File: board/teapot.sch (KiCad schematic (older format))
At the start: 31 parts

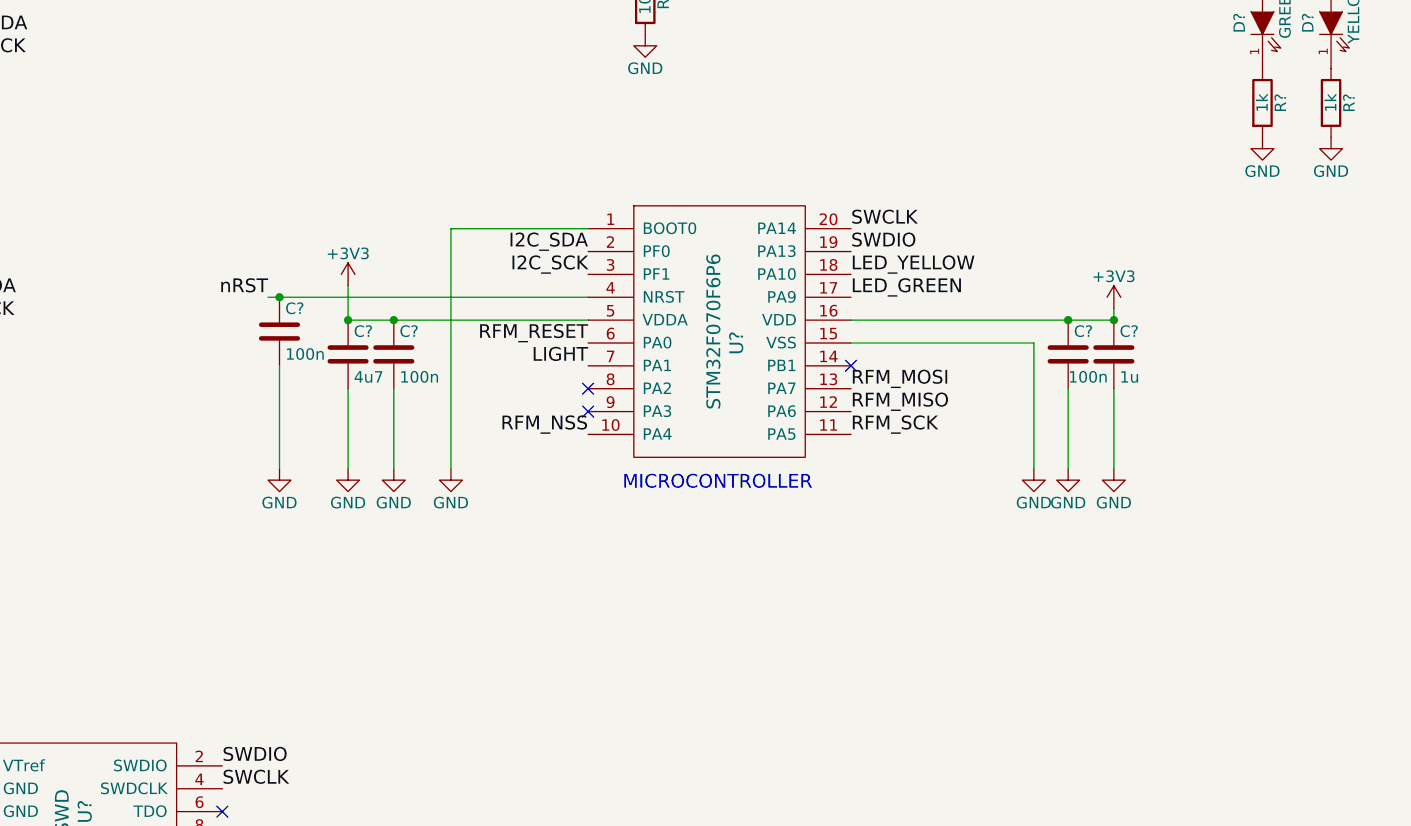
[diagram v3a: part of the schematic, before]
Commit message: Changed stm32f070 to stm32l052k8u6
Also did mcu decouplers properly
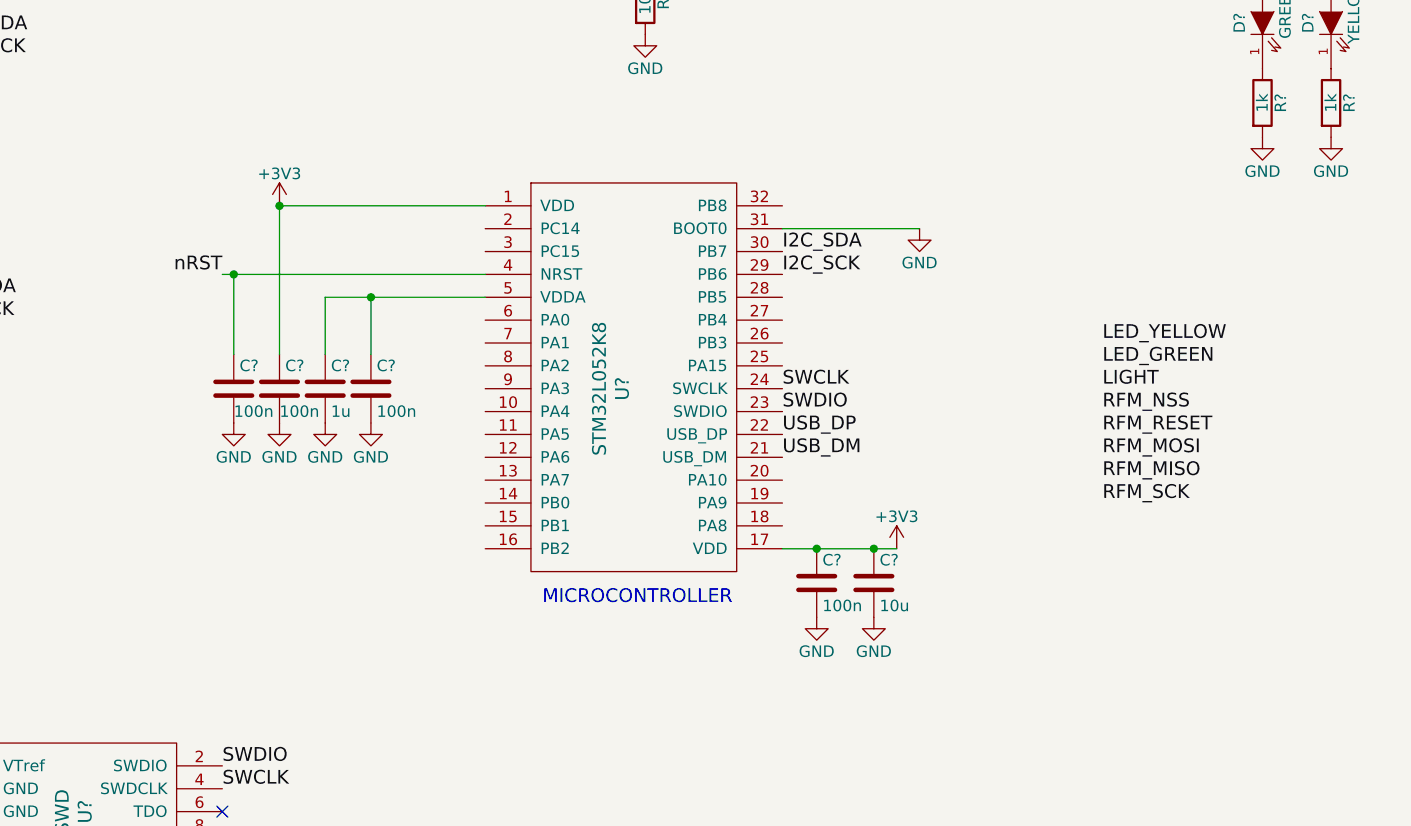
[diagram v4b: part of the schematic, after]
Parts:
- removed C? (x3): 100n, symbol C
- removed C?: 1u, symbol C
- removed C?: 4u7, symbol C
- removed U?: STM32F070F6P6, symbol STM32F070F6P6
- added C? (x4): 100n, symbol C
- added C?: 10u, symbol C
- added C?: 1u, symbol C
- added U?: STM32L052K8, symbol STM32L052K8
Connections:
- net +3V3: now also C?.1, C?.1, C?.1, U?.1 (VDD), U?.17 (VDD)
- net GND: now also C?.2, C?.2, C?.2, C?.2, C?.2, C?.2, U?.31 (BOOT0)
- net I2C_SCK: now also U?.29 (PB6)
- net I2C_SDA: now also U?.30 (PB7)
- net SWCLK: now also U?.24 (SWCLK)
- net SWDIO: now also U?.23 (SWDIO)
- net nRST: now also C?.1, U?.4 (NRST)
- new net: C?.1, C?.1, U?.5 (VDDA)
- new net USB_DM: U?.21 (USB_DM)
- new net USB_DP: U?.22 (USB_DP)
- no-connect marks 11 -> 8

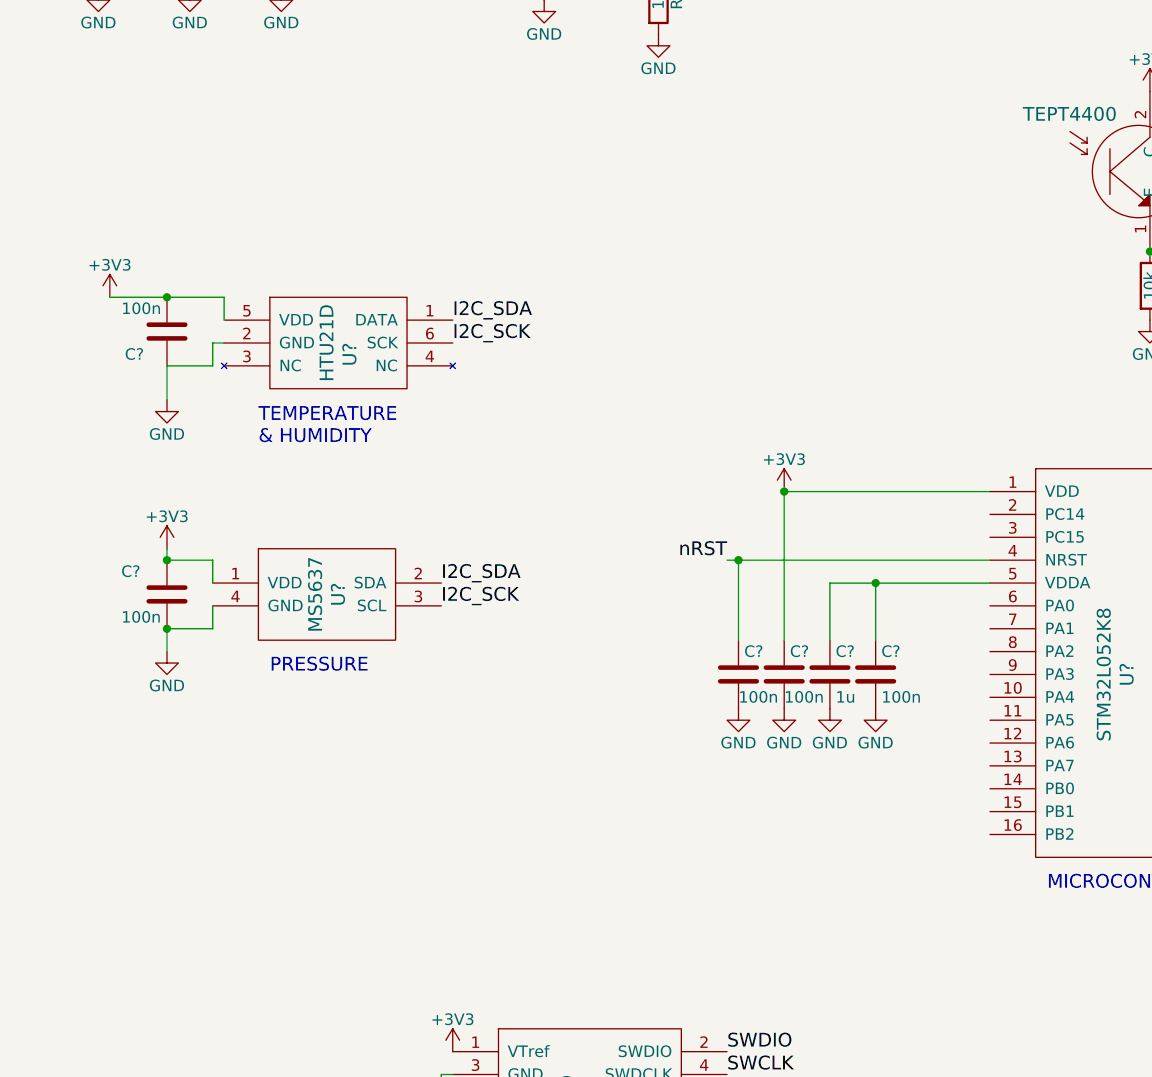
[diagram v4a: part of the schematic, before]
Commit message: Added watch crystal
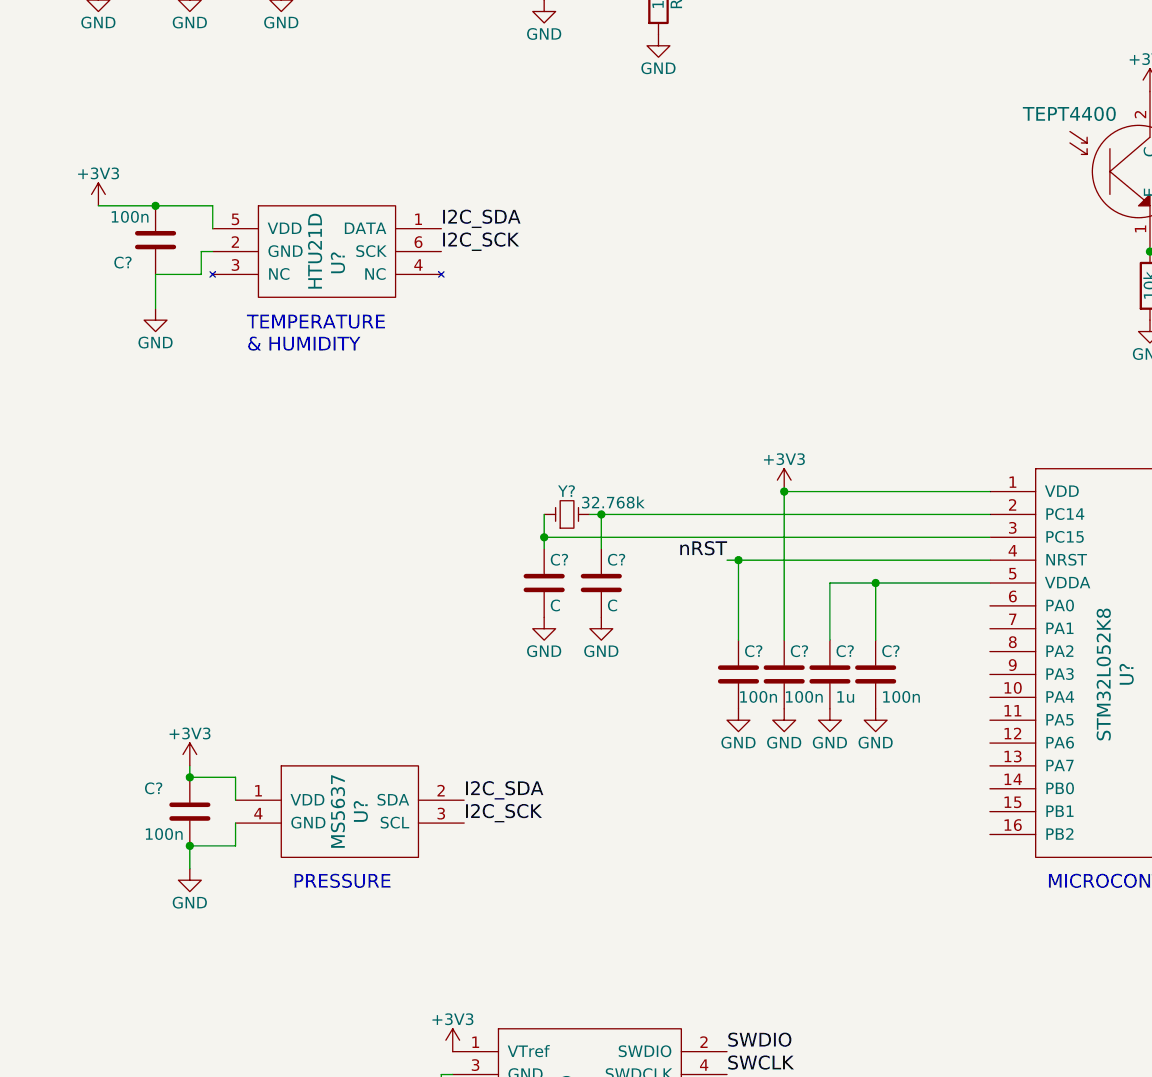
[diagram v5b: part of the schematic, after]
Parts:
- added C? (x2): C, symbol C
- added Y?: 32.768k, symbol Crystal_Small
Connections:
- net GND: now also C?.2, C?.2
- net at U?.2 (PC14): now also C?.1, Y?.2
- net at U?.3 (PC15): now also C?.1, Y?.1
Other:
- moved on the sheet: C?, U?
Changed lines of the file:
@@
 L C C?
 U 1 1 56707B80
-P 1300 3250
-F 0 "C?" H 1400 3350 50  0000 L CNN
-F 1 "100n" H 1325 3150 50  0000 L CNN
-F 2 "" H 1338 3100 50  0000 C CNN
-F 3 "" H 1300 3250 50  0000 C CNN
-	1    1300 3250
+P 1250 2850
+F 0 "C?" H 1350 2950 50  0000 L CNN
+F 1 "100n" H 1275 2750 50  0000 L CNN
+F 2 "" H 1288 2700 50  0000 C CNN
+F 3 "" H 1250 2850 50  0000 C CNN
+	1    1250 2850
 	-1   0    0    1
 $EndComp
@@
 L HTU21D U?
 U 1 1 5670851D
-P 2050 3300
-F 0 "U?" V 2100 3250 60  0000 C CNN
-F 1 "HTU21D" V 2000 3300 60  0000 C CNN
-F 2 "" H 2100 3350 60  0000 C CNN
-F 3 "" H 2100 3350 60  0000 C CNN
-F 4 "2393536" H 2050 3300 60  0001 C CNN "Farnell"
-	1    2050 3300
+P 2000 2900
+F 0 "U?" V 2050 2850 60  0000 C CNN
+F 1 "HTU21D" V 1950 2900 60  0000 C CNN
+F 2 "" H 2050 2950 60  0000 C CNN
+F 3 "" H 2050 2950 60  0000 C CNN
+F 4 "2393536" H 2000 2900 60  0001 C CNN "Farnell"
+	1    2000 2900
 	1    0    0    -1
 $EndComp
@@
 L +3V3 #PWR?
 U 1 1 56708637
-P 1050 3100
-F 0 "#PWR?" H 1050 2950 50  0001 C CNN
-F 1 "+3V3" H 1050 3240 50  0000 C CNN
-F 2 "" H 1050 3100 50  0000 C CNN
-F 3 "" H 1050 3100 50  0000 C CNN
-	1    1050 3100
+P 1000 2700
+F 0 "#PWR?" H 1000 2550 50  0001 C CNN
+F 1 "+3V3" H 1000 2840 50  0000 C CNN
+F 2 "" H 1000 2700 50  0000 C CNN
+F 3 "" H 1000 2700 50  0000 C CNN
+	1    1000 2700
 	1    0    0    -1
 $EndComp
@@
 L GND #PWR?
 U 1 1 5670867A
-P 1300 3550
-F 0 "#PWR?" H 1300 3300 50  0001 C CNN
-F 1 "GND" H 1300 3400 50  0000 C CNN
-F 2 "" H 1300 3550 50  0000 C CNN
-F 3 "" H 1300 3550 50  0000 C CNN
-	1    1300 3550
+P 1250 3150
+F 0 "#PWR?" H 1250 2900 50  0001 C CNN
+F 1 "GND" H 1250 3000 50  0000 C CNN
+F 2 "" H 1250 3150 50  0000 C CNN
+F 3 "" H 1250 3150 50  0000 C CNN
+	1    1250 3150
 	1    0    0    -1
 $EndComp
@@
 L MS5637 U?
 U 1 1 56708DE8
-P 2000 4400
-F 0 "U?" V 2050 4400 60  0000 C CNN
-F 1 "MS5637" V 1950 4400 60  0000 C CNN
-F 2 "" H 1900 4550 60  0000 C CNN
-F 3 "" H 1900 4550 60  0000 C CNN
-	1    2000 4400
+P 2100 5350
+F 0 "U?" V 2150 5350 60  0000 C CNN
+F 1 "MS5637" V 2050 5350 60  0000 C CNN
+F 2 "" H 2000 5500 60  0000 C CNN
+F 3 "" H 2000 5500 60  0000 C CNN
+	1    2100 5350
 	1    0    0    -1
 $EndComp
@@
 L C C?
 U 1 1 56708EC5
-P 1300 4400
-F 0 "C?" H 1100 4500 50  0000 L CNN
-F 1 "100n" H 1100 4300 50  0000 L CNN
-F 2 "" H 1338 4250 50  0000 C CNN
-F 3 "" H 1300 4400 50  0000 C CNN
-	1    1300 4400
+P 1400 5350
+F 0 "C?" H 1200 5450 50  0000 L CNN
+F 1 "100n" H 1200 5250 50  0000 L CNN
+F 2 "" H 1438 5200 50  0000 C CNN
+F 3 "" H 1400 5350 50  0000 C CNN
+	1    1400 5350
 	1    0    0    -1
 $EndComp
@@
 L +3V3 #PWR?
 U 1 1 56708F0F
-P 1300 4200
-F 0 "#PWR?" H 1300 4050 50  0001 C CNN
-F 1 "+3V3" H 1300 4340 50  0000 C CNN
-F 2 "" H 1300 4200 50  0000 C CNN
-F 3 "" H 1300 4200 50  0000 C CNN
-	1    1300 4200
+P 1400 5150
+F 0 "#PWR?" H 1400 5000 50  0001 C CNN
+F 1 "+3V3" H 1400 5290 50  0000 C CNN
+F 2 "" H 1400 5150 50  0000 C CNN
+F 3 "" H 1400 5150 50  0000 C CNN
+	1    1400 5150
 	1    0    0    -1
 $EndComp
@@
 L GND #PWR?
 U 1 1 56708F9A
-P 1300 4650
-F 0 "#PWR?" H 1300 4400 50  0001 C CNN
-F 1 "GND" H 1300 4500 50  0000 C CNN
-F 2 "" H 1300 4650 50  0000 C CNN
-F 3 "" H 1300 4650 50  0000 C CNN
-	1    1300 4650
+P 1400 5600
+F 0 "#PWR?" H 1400 5350 50  0001 C CNN
+F 1 "GND" H 1400 5450 50  0000 C CNN
+F 2 "" H 1400 5600 50  0000 C CNN
+F 3 "" H 1400 5600 50  0000 C CNN
+	1    1400 5600
 	1    0    0    -1
 $EndComp
@@
 	1    0    0    -1
 $EndComp
-Text Notes 1750 4750 0    60   ~ 0
+Text Notes 1850 5700 0    60   ~ 0
 PRESSURE
-Text Notes 1700 3750 0    60   ~ 0
+Text Notes 1650 3350 0    60   ~ 0
 TEMPERATURE\n& HUMIDITY
 Text Notes 2000 1800 0    60   ~ 0
@@
 	1    0    0    -1
 $EndComp
-Text Label 2550 3200 0    60   ~ 0
+Text Label 2500 2800 0    60   ~ 0
 I2C_SDA
-Text Label 2550 3300 0    60   ~ 0
+Text Label 2500 2900 0    60   ~ 0
 I2C_SCK
-Text Label 2500 4350 0    60   ~ 0
+Text Label 2600 5300 0    60   ~ 0
 I2C_SDA
-Text Label 2500 4450 0    60   ~ 0
+Text Label 2600 5400 0    60   ~ 0
 I2C_SCK
 Text Label 6000 1250 0    60   ~ 0
@@
 Connection ~ 1000 1600
 Wire Wire Line
-	1050 3100 1550 3100
-Wire Wire Line
-	1550 3100 1550 3200
-Wire Wire Line
-	1300 3400 1500 3400
-Wire Wire Line
-	1500 3400 1500 3300
-Wire Wire Line
-	1500 3300 1550 3300
-Connection ~ 1300 3100
-Wire Wire Line
-	1300 3400 1300 3550
+	1000 2700 1500 2700
+Wire Wire Line
+	1500 2700 1500 2800
+Wire Wire Line
+	1250 3000 1450 3000
+Wire Wire Line
+	1450 3000 1450 2900
+Wire Wire Line
+	1450 2900 1500 2900
+Connection ~ 1250 2700
+Wire Wire Line
+	1250 3000 1250 3150
 Wire Wire Line
 	6000 1250 5900 1250
@@
 	5900 850  5900 900
 Wire Wire Line
-	1300 4200 1300 4250
-Wire Wire Line
-	1300 4250 1500 4250
-Wire Wire Line
-	1500 4250 1500 4350
-Connection ~ 1300 4250
-Wire Wire Line
-	1300 4550 1300 4650
-Wire Wire Line
-	1500 4450 1500 4550
-Wire Wire Line
-	1500 4550 1300 4550
-Connection ~ 1300 4550
+	1400 5150 1400 5200
+Wire Wire Line
+	1400 5200 1600 5200
+Wire Wire Line
+	1600 5200 1600 5300
+Connection ~ 1400 5200
+Wire Wire Line
+	1400 5500 1400 5600
+Wire Wire Line
+	1600 5400 1600 5500
+Wire Wire Line
+	1600 5500 1400 5500
+Connection ~ 1400 5500
 Wire Wire Line
 	5600 2900 5850 2900
@@
 	1    0    0    -1
 $EndComp
+$Comp
+L Crystal_Small Y?
+U 1 1 56762471
+P 3050 4050
+F 0 "Y?" H 3050 4150 50  0000 C CNN
+F 1 "32.768k" H 3250 4100 50  0000 C CNN
+F 2 "" H 3050 4050 50  0000 C CNN
+F 3 "http://www.farnell.com/datasheets/1883680.pdf" H 3050 4050 50  0001 C CNN
+F 4 "2101347" H 3050 4050 60  0001 C CNN "Farnell"
+	1    3050 4050
+	1    0    0    -1
+$EndComp
+Wire Wire Line
+	3150 4050 4900 4050
+Wire Wire Line
+	2950 4050 2950 4200
+$Comp
+L C C?
+U 1 1 56762810
+P 2950 4350
+F 0 "C?" H 2975 4450 50  0000 L CNN
+F 1 "C" H 2975 4250 50  0000 L CNN
+F 2 "" H 2988 4200 50  0000 C CNN
+F 3 "" H 2950 4350 50  0000 C CNN
+	1    2950 4350
+	1    0    0    -1
+$EndComp
+$Comp
+L GND #PWR?
+U 1 1 56762871
+P 2950 4500
+F 0 "#PWR?" H 2950 4250 50  0001 C CNN
+F 1 "GND" H 2950 4350 50  0000 C CNN
+F 2 "" H 2950 4500 50  0000 C CNN
+F 3 "" H 2950 4500 50  0000 C CNN
+	1    2950 4500
+	1    0    0    -1
+$EndComp
+$Comp
+L C C?
+U 1 1 567628C9
+P 3200 4350
+F 0 "C?" H 3225 4450 50  0000 L CNN
+F 1 "C" H 3225 4250 50  0000 L CNN
+F 2 "" H 3238 4200 50  0000 C CNN
+F 3 "" H 3200 4350 50  0000 C CNN
+	1    3200 4350
+	1    0    0    -1
+$EndComp
+Wire Wire Line
+	2950 4150 4900 4150
+Connection ~ 2950 4150
+Wire Wire Line
+	3200 4200 3200 4050
+Connection ~ 3200 4050
+$Comp
+L GND #PWR?
+U 1 1 56762B31
+P 3200 4500
+F 0 "#PWR?" H 3200 4250 50  0001 C CNN
+F 1 "GND" H 3200 4350 50  0000 C CNN
+F 2 "" H 3200 4500 50  0000 C CNN
+F 3 "" H 3200 4500 50  0000 C CNN
+	1    3200 4500
+	1    0    0    -1
+$EndComp
